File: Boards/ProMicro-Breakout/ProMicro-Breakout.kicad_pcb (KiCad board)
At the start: 2 copper layers, 81.3 x 54.6 mm, 32 parts, among them J1 Conn_01x04, J10 Conn_01x12, J11 Conn_01x04, J12 Conn_01x04, J13 Conn_01x02, J14 Conn_01x04, J2 Conn_01x04, J3 Conn_01x04, J4 Conn_01x04, J5 Conn_01x04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

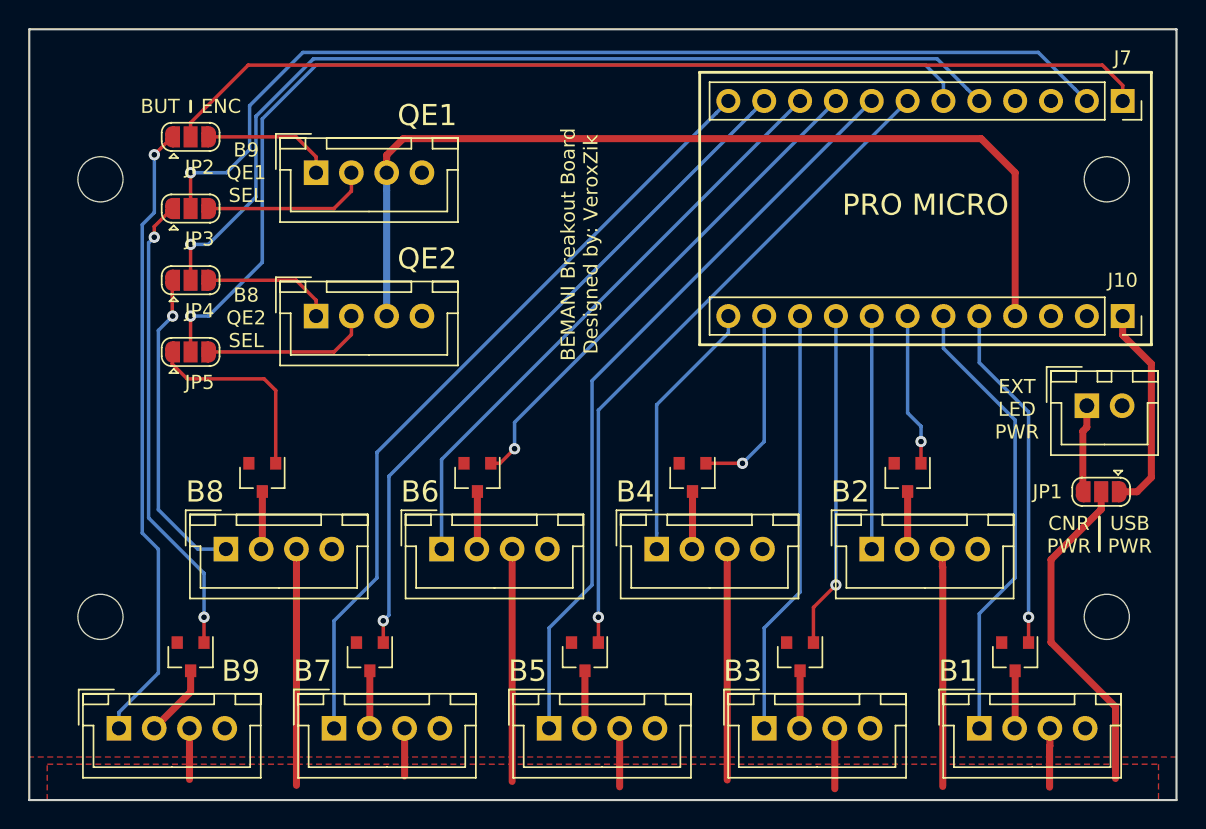
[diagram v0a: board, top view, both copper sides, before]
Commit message: Update ProMicro-Breakout board.
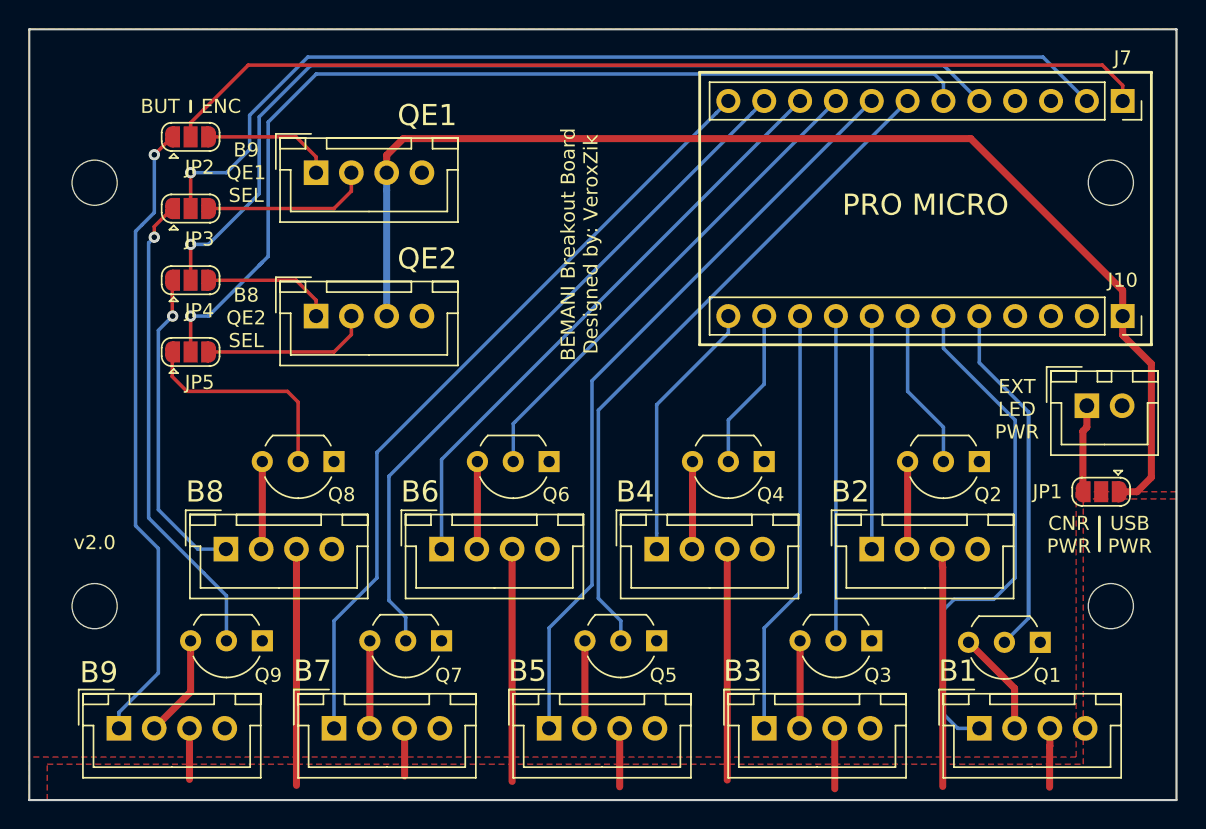
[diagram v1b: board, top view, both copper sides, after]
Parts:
- Q1, Q2, Q3, Q4, Q5, Q6, Q7, Q8, Q9: value Si2302CDS -> 2N7000; footprint TO_SOT_Packages_SMD:SOT-23 -> Package_TO_SOT_THT:TO-92_Inline_Wide
- moved Q3 5.20 mm to (162.6, 131.0), turned to 180 degrees
- moved Q7 5.20 mm to (132.1, 131.0), turned to 180 degrees
- moved Q2 5.20 mm to (170.2, 118.3), turned to 180 degrees
- moved Q9 5.20 mm to (119.4, 131.0), turned to 180 degrees
- moved Q8 5.20 mm to (124.5, 118.3), turned to 180 degrees
- moved Q5 5.20 mm to (147.3, 131.0), turned to 180 degrees
- moved Q4 5.20 mm to (154.9, 118.3), turned to 180 degrees
- moved Q6 5.20 mm to (139.7, 118.3), turned to 180 degrees
- moved Q1 2.05 mm to (174.5, 131.1), turned to 180 degrees
- moved MH1 0.86 mm to (107.5, 128.5)
- moved MH3 0.81 mm to (179.5, 128.5)
- moved MH2 0.48 mm to (107.5, 98.5)
- moved MH4 0.37 mm to (179.5, 98.5)
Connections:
- J1 pad 3: +5V -> VBUS
- J10 pad 3: Net-(J10-Pad3) -> unconnected-(J10-Pad3)
- J2 pad 3: +5V -> VBUS
- Q1 pad 1: /B1LED -> GND
- Q1 pad 2: GND -> /B1LED
- Q2 pad 1: /B2LED -> GND
- Q2 pad 2: GND -> /B2LED
- Q3 pad 1: /B3LED -> GND
- Q3 pad 2: GND -> /B3LED
- Q4 pad 1: /B4LED -> GND
- Q4 pad 2: GND -> /B4LED
- Q5 pad 1: /B5LED -> GND
- Q5 pad 2: GND -> /B5LED
- Q6 pad 1: /B6LED -> GND
- Q6 pad 2: GND -> /B6LED
- Q7 pad 1: /B7LED -> GND
- Q7 pad 2: GND -> /B7LED
- Q8 pad 1: /B8LED -> GND
- Q8 pad 2: GND -> /B8LED
- Q9 pad 1: /B9LED -> GND
- Q9 pad 2: GND -> /B9LED
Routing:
- net VBUS: track 14.9 -> 85.3 mm
- net +5V: track 67.6 -> 0.00 mm
- net /LED+: track 109.7 -> 86.0 mm
- net /B1LED: track 24.6 -> 39.8 mm, vias 1 -> 0
- net /B1: track 32.4 -> 37.0 mm
- net Net-(J3-Pad2): track 4.10 -> 7.50 mm
- net /B4LED: track 13.7 -> 11.4 mm, vias 1 -> 0
- net Net-(J8-Pad2): track 4.10 -> 6.22 mm
- net Net-(J5-Pad2): track 4.10 -> 6.22 mm
- net Net-(J14-Pad2): track 5.21 -> 7.33 mm
- net Net-(J11-Pad2): track 4.10 -> 6.22 mm
- net Net-(J9-Pad2): track 4.10 -> 6.22 mm
- net Net-(J6-Pad2): track 4.10 -> 6.22 mm
- net Net-(J4-Pad2): track 4.10 -> 6.22 mm
- net Net-(J12-Pad2): track 4.11 -> 6.24 mm
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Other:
- net class Default removed
- rule pad_to_mask_clearance: 0.2 -> 0
- board text added: "v2.0"
